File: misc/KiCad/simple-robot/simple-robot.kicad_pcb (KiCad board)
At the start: 2 copper layers, 130 x 81 mm, 38 parts, among them J1 Conn_01x03_Pin, J2 Conn_01x03_Pin, J3 Conn_01x03_Pin, U1 Pico2

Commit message: schematic v2
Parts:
- removed ?: , 
- added C9: 100nF_Ceramic, Capacitor_THT:C_Disc_D5.0mm_W2.5mm_P2.50mm, F.Cu at (63.5, 71.0)
- added J4: Conn_01x03_Pin, Connector_PinHeader_2.54mm:PinHeader_1x03_P2.54mm_Vertical, F.Cu at (57.5, 68.5)
- added REF-MNT: MountingHole_3.7mm_Pad, MountingHole:MountingHole_3.7mm_Pad, F.Cu at (148.5, 105.0)
- moved OLED1 40.1 mm to (130.5, 119.1)
- moved C6 40.0 mm to (126.5, 109.0)
- moved R1 36.3 mm to (146.5, 86.9), turned to 90 degrees
- moved IMU1 36.3 mm to (120.4, 74.0), turned to 180 degrees
- moved C5 32.5 mm to (135.0, 94.5)
- moved TP1 32.0 mm to (133.2, 108.7)
- moved C8 30.6 mm to (131.2, 96.5)
- moved LS_1 30.6 mm to (124.4, 101.7)
- moved C7 29.6 mm to (112.5, 95.5)
- moved BATT1 27.2 mm to (112.8, 113.8), turned to -90 degrees
- moved TP2 23.2 mm to (137.5, 108.8)
- moved C4 20.2 mm to (133.8, 81.5), turned to -90 degrees
- moved C2 15.0 mm to (112.0, 120.0)
- moved C3 14.8 mm to (112.2, 130.8)
- moved S5V1 11.6 mm to (99.7, 121.5)
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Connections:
- U1 pad 7: unconnected-(U1-GPIO5-Pad7)_1 -> Net-(J4-Pin_1)
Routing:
- net Net-(LS_1-LV1): track 253.7 -> 23.8 mm, vias 8 -> 0
- net Net-(LS_1-LV2): track 122.6 -> 18.6 mm, vias 2 -> 0
- net Net-(ENCA1-Pin_3): track 232.1 -> 167.7 mm, vias 2 -> 0
- net Net-(MD1-PWMB): track 113.0 -> 60.3 mm, vias 1 -> 0
- net Net-(IMU1-SCL): track 140.1 -> 88.7 mm, vias 2 -> 0
- net Net-(LS_1-LV4): track 83.2 -> 33.4 mm
- net Net-(IMU1-VCC): track 233.8 -> 199.8 mm, vias 1 -> 2
- net Net-(J4-Pin_1): track 0.00 -> 32.9 mm
- net Net-(LS_1-HV2): track 51.4 -> 20.0 mm, vias 2 -> 0
- net Net-(IMU1-SDA): track 126.5 -> 97.8 mm, vias 3 -> 0
- net Net-(LS_1-HV1): track 52.2 -> 24.4 mm, vias 1 -> 0
- net Net-(LS_1-LV3): track 60.9 -> 33.7 mm, vias 4 -> 0
- net Net-(IMU1-ADD): track 64.1 -> 41.6 mm
- net Net-(MD1-A01): track 48.0 -> 28.4 mm
- net +3V8: track 109.2 -> 90.4 mm
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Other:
- board size 130 x 81 mm -> 99.8 x 81 mm
- board text added: "PWM"
- board text added: "REC"
- board text added: "Servo"
- board text added: "simple-robot 01-2025 rafael v0.2"
- board text removed: "simple-robot 01-2025 rafael v0.1"

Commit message: update schematic and pcb
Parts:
- moved BATT1 37.5 mm to (148.5, 125.2), turned to 0 degrees
- moved C5 8.11 mm to (139.5, 87.8)
- moved C7 4.78 mm to (113.0, 90.8)
- moved R1 3.49 mm to (146.5, 90.4)
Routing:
- net +3V8: track 90.4 -> 138.3 mm, vias 0 -> 2
- net Net-(ENCA1-Pin_3): track 167.7 -> 183.6 mm, vias 0 -> 1
- net Net-(LS_1-HV1): track 24.4 -> 18.2 mm
- net Net-(LS_1-HV4): track 37.0 -> 33.6 mm, vias 1 -> 3
- net Net-(LS_1-HV3): track 31.2 -> 34.3 mm, vias 0 -> 3
- net Net-(MD1-BIN2): track 37.1 -> 39.9 mm
- net Net-(MD1-A02): track 28.4 -> 30.9 mm
- net Net-(MD1-A01): track 28.4 -> 30.8 mm, vias 0 -> 1
- net Net-(LS_1-HV2): track 20.0 -> 22.1 mm
- net Net-(IMU1-VCC): track 199.8 -> 201.8 mm, vias 2 -> 5
- net Net-(MD1-PWMB): track 60.3 -> 62.0 mm
- net Net-(IMU1-SCL): track 88.7 -> 89.9 mm, vias 0 -> 3
- net Net-(MD1-BIN1): track 48.5 -> 49.6 mm
- net Net-(U1-GPIO2): track 19.0 -> 18.1 mm
- net Net-(MD1-AIN2): track 31.9 -> 32.7 mm
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- added copper zone on B.Cu, net GND
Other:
- board text added: "simple-robot 01-2025 v0.3 rafael"
- board text removed: "simple-robot 01-2025 rafael v0.2"

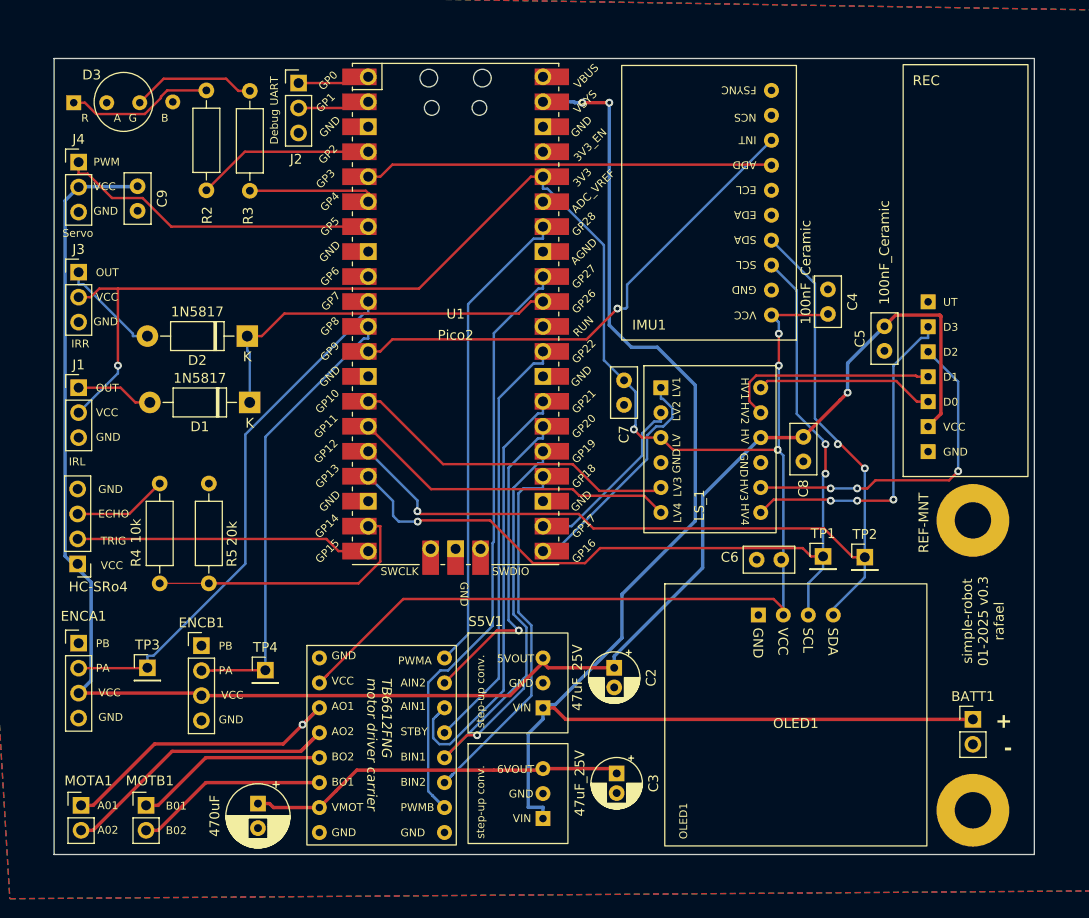
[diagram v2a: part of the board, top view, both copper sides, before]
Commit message: update 3d models for hc-sr04 mount, update KiCad files, update schematic and PCB
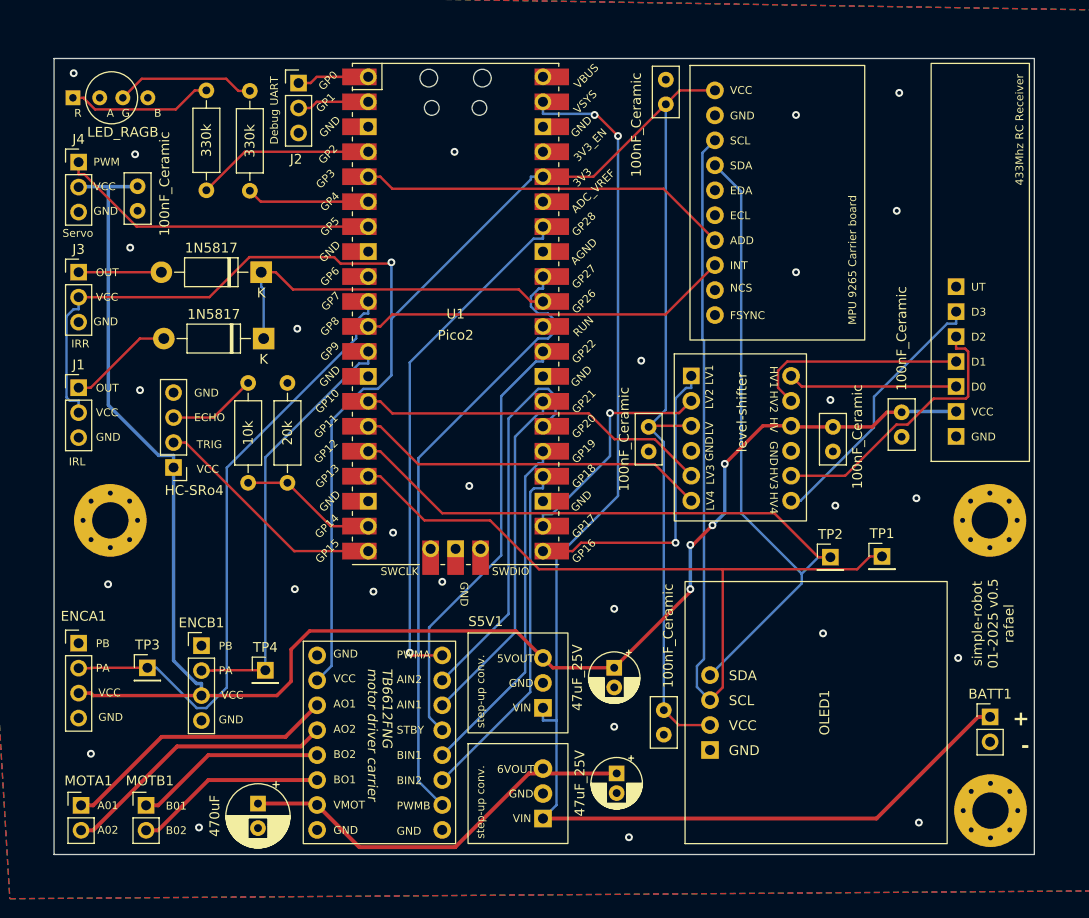
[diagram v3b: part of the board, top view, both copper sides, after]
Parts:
- removed REF**, REF-MNT: MountingHole_3.7mm_Pad, MountingHole:MountingHole_3.7mm_Pad
- added H1: MountingHole_Pad, MountingHole:MountingHole_3.7mm_Pad_Via, F.Cu at (60.7, 105.0)
- added H2: MountingHole_Pad, MountingHole:MountingHole_3.7mm_Pad_Via, F.Cu at (150.3, 134.5)
- added H3: MountingHole_Pad, MountingHole:MountingHole_3.7mm_Pad_Via, F.Cu at (150.2, 105.0)
- moved C4 27.0 mm to (117.2, 60.2)
- moved C6 20.2 mm to (117.0, 126.8), turned to 90 degrees
- moved HC-SRo4 13.8 mm to (67.2, 99.6)
- moved R4 13.6 mm to (74.8, 91.0)
- moved R5 13.0 mm to (78.8, 101.2)
- moved IMU1 9.82 mm to (129.9, 71.4), turned to 0 degrees
- moved C5 8.92 mm to (141.2, 96.5)
- moved D1 6.65 mm to (76.3, 86.5)
- moved D2 6.65 mm to (76.1, 79.8)
- moved OLED1 6.58 mm to (126.8, 124.6), turned to 90 degrees
- moved TP1 6.00 mm to (139.2, 108.7)
- moved C7 5.36 mm to (115.5, 95.5)
- moved TP2 3.50 mm to (134.0, 108.8)
- moved LS_1 3.31 mm to (127.5, 100.5)
- moved R1 3.24 mm to (149.3, 88.8)
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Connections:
- U1 pad 11: Net-(ENCB1-Pin_2) -> Net-(IMU1-INT)
- U1 pad 12: Net-(IMU1-INT) -> Net-(ENCB1-Pin_2)
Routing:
- net Net-(IMU1-SCL): track 89.9 -> 129.0 mm, vias 3 -> 0
- net Net-(IMU1-SDA): track 98.6 -> 114.5 mm, vias 3 -> 0
- net Net-(U1-GPIO14): track 28.2 -> 14.0 mm
- net Net-(MD1-BIN1): track 49.6 -> 35.4 mm, vias 1 -> 0
- net Net-(IMU1-INT): track 51.3 -> 37.9 mm, vias 1 -> 0
- net Net-(MD1-AIN1): track 45.6 -> 35.4 mm
- net Net-(ENCA1-Pin_2): track 54.2 -> 63.2 mm
- net Net-(ENCA1-Pin_3): track 183.6 -> 175.2 mm, vias 1 -> 4
- net Net-(LS_1-LV1): track 23.8 -> 31.8 mm, vias 0 -> 1
- net Net-(IMU1-VCC): track 201.8 -> 209.4 mm, vias 5 -> 1
- net Net-(MD1-AIN2): track 32.7 -> 39.4 mm, vias 1 -> 0
- net Net-(LS_1-HV4): track 33.6 -> 27.3 mm, vias 3 -> 0
- net Net-(LS_1-HV3): track 34.3 -> 28.5 mm, vias 3 -> 0
- net Net-(HC-SRo4-Pin_2): track 30.1 -> 24.4 mm
- net Net-(LS_1-LV2): track 18.6 -> 23.7 mm, vias 0 -> 1
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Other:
- board text added: "433Mhz RC Receiver"
- board text added: "MPU 9265 Carrier board"
- board text added: "level-shifter"
- board text added: "simple-robot 01-2025 v0.5 rafael"
- board text removed: "REC"
- board text removed: "simple-robot 01-2025 v0.3 rafael"

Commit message: Update KiCad project files and remove unnecessary autosave and lock files
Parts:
- removed C7: 100nF_Ceramic, Capacitor_THT:C_Disc_D5.0mm_W2.5mm_P2.50mm
- removed D1, D2: 1N5817, Diode_THT:D_DO-41_SOD81_P10.16mm_Horizontal
- removed J1, J2, J3, J4: Conn_01x03_Pin, Connector_PinHeader_2.54mm:PinHeader_1x03_P2.54mm_Vertical
- removed R4: 10k, Resistor_THT:R_Axial_DIN0207_L6.3mm_D2.5mm_P10.16mm_Horizontal
- removed R5: 20k, Resistor_THT:R_Axial_DIN0207_L6.3mm_D2.5mm_P10.16mm_Horizontal
- removed TP1, TP2, TP3, TP4: Conn_01x01_Pin, Connector_PinHeader_2.54mm:PinHeader_1x01_P2.54mm_Vertical
- added C10: 100nF, Capacitor_THT:C_Disc_D5.0mm_W2.5mm_P2.50mm, F.Cu at (57.6, 94.2)
- added C11: 100nF, Capacitor_THT:C_Disc_D5.0mm_W2.5mm_P2.50mm, F.Cu at (67.0, 125.2)
- added C12: 100nF_Ceramic, Capacitor_THT:C_Disc_D5.0mm_W2.5mm_P2.50mm, F.Cu at (63.5, 125.2)
- added C13: 100nF, Capacitor_THT:C_Disc_D5.0mm_W2.5mm_P2.50mm, F.Cu at (80.8, 83.8)
- added C14: 100nF, Capacitor_THT:C_Disc_D5.0mm_W2.5mm_P2.50mm, F.Cu at (63.8, 83.5)
- added C15: 100nF, Capacitor_THT:C_Disc_D5.0mm_W2.5mm_P2.50mm, F.Cu at (78.2, 121.2)
- added C17: 220uF_10V, Capacitor_THT:CP_Radial_D6.3mm_P2.50mm, F.Cu at (111.5, 118.8)
- added DBG1: Conn_01x03_Pin, Connector_PinHeader_2.54mm:PinHeader_1x03_P2.54mm_Vertical, F.Cu at (80.5, 60.2)
- added IRL1: Conn_01x03_Pin, Connector_PinHeader_2.54mm:PinHeader_1x03_P2.54mm_Vertical, F.Cu at (67.2, 99.5)
- added IRR1: Conn_01x03_Pin, Connector_PinHeader_2.54mm:PinHeader_1x03_P2.54mm_Vertical, F.Cu at (74.0, 99.5)
- added LS_2: ~, common-hobby-things:Level shifter 4 bi-dir, F.Cu at (75.0, 88.7)
- added SERVO1: Conn_01x03_Pin, Connector_PinHeader_2.54mm:PinHeader_1x03_P2.54mm_Vertical, F.Cu at (57.2, 68.5)
- added TPENCA1: Conn_01x01_Pin, Connector_PinHeader_2.54mm:PinHeader_1x01_P2.54mm_Vertical, F.Cu at (57.8, 112.5)
- added TPENCB1: Conn_01x01_Pin, Connector_PinHeader_2.54mm:PinHeader_1x01_P2.54mm_Vertical, F.Cu at (70.8, 112.8)
- added TPGND1: Conn_01x01_Pin, Connector_PinHeader_2.54mm:PinHeader_1x01_P2.54mm_Vertical, F.Cu at (71.8, 130.5)
- added TPGND2: Conn_01x01_Pin, Connector_PinHeader_2.54mm:PinHeader_1x01_P2.54mm_Vertical, F.Cu at (141.0, 62.0)
- added TPSCL1: Conn_01x01_Pin, Connector_PinHeader_2.54mm:PinHeader_1x01_P2.54mm_Vertical, F.Cu at (120.5, 109.0)
- added TPSDA1: Conn_01x01_Pin, Connector_PinHeader_2.54mm:PinHeader_1x01_P2.54mm_Vertical, F.Cu at (127.0, 109.0)
- C2: value 47uF_25V -> 220uF_10V; footprint Capacitor_THT:CP_Radial_D5.0mm_P2.00mm -> Capacitor_THT:CP_Radial_D6.3mm_P2.50mm
- C3: value 47uF_25V -> 100nF; footprint Capacitor_THT:CP_Radial_D5.0mm_P2.00mm -> Capacitor_THT:C_Disc_D5.0mm_W2.5mm_P2.50mm
- C4, C5, C6, C8, C9: value 100nF_Ceramic -> 100nF
- moved C3 41.4 mm to (134.0, 95.5)
- moved C8 18.8 mm to (115.5, 95.2)
- moved HC-SRo4 16.1 mm to (57.5, 86.8)
- moved R3 11.3 mm to (77.6, 60.5), turned to 180 degrees
- moved C2 10.6 mm to (111.5, 130.6)
- moved R2 9.57 mm to (77.5, 64.9), turned to 180 degrees
- moved OLED1 1.35 mm to (125.6, 125.1)
- moved C6 1.06 mm to (116.0, 127.0)
- moved ENCB1 0.75 mm to (70.8, 117.8)
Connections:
- C2 pad 1: Net-(ENCA1-Pin_3) -> Net-(MD1-VMOT)
- C3 pad 1: Net-(MD1-VMOT) -> Net-(ENCA1-Pin_3)
- C4 pad 1: GND -> Net-(IMU1-VCC)
- C4 pad 2: Net-(IMU1-VCC) -> GND
- C5 pad 1: GND -> Net-(ENCA1-Pin_3)
- C5 pad 2: Net-(ENCA1-Pin_3) -> GND
- C8 pad 1: Net-(ENCA1-Pin_3) -> Net-(IMU1-VCC)
- MOTB1 pad 1: Net-(MD1-B02) -> Net-(MD1-B01)
- MOTB1 pad 2: Net-(MD1-B01) -> Net-(MD1-B02)
- R1 pad 3: Net-(LS_1-HV1) -> Net-(LS_1-HV4)
- R1 pad 4: Net-(LS_1-HV2) -> Net-(LS_1-HV3)
- R1 pad 5: Net-(LS_1-HV3) -> Net-(LS_1-HV2)
- R1 pad 6: Net-(LS_1-HV4) -> Net-(LS_1-HV1)
- U1 pad 10: Net-(ENCA1-Pin_2) -> Net-(LS_2-LV2)
- U1 pad 12: Net-(ENCB1-Pin_2) -> Net-(LS_2-LV1)
- U1 pad 13: unconnected-(U1-GND-Pad13) -> GND
- U1 pad 14: Net-(LS_1-LV3) -> Net-(LS_1-LV4)
- U1 pad 15: Net-(LS_1-LV4) -> Net-(LS_1-LV2)
- U1 pad 20: Net-(HC-SRo4-Pin_2) -> Net-(LS_2-LV4)
- U1 pad 21: Net-(LS_1-LV1) -> Net-(LS_1-LV3)
- U1 pad 22: Net-(LS_1-LV2) -> Net-(LS_1-LV1)
- U1 pad 28: unconnected-(U1-GND-Pad28)_1 -> GND
- U1 pad 42: GND -> unconnected-(U1-GND-Pad42)_1
- U1 pad 8: unconnected-(U1-GND-Pad8) -> GND
- U1 pad 9: unconnected-(U1-GPIO6-Pad9)_1 -> Net-(IRL1-Pin_1)
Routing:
- net Net-(IRL1-Pin_1): track 0.00 -> 39.2 mm, vias 0 -> 1
- net Net-(LS_2-LV4): track 0.00 -> 33.7 mm, vias 0 -> 1
- net Net-(IMU1-SCL): track 129.0 -> 96.8 mm
- net Net-(LS_2-LV1): track 0.00 -> 27.1 mm
- net Net-(LS_2-LV2): track 0.00 -> 24.2 mm, vias 0 -> 1
- net Net-(LS_2-LV3): track 14.0 -> 35.2 mm, vias 0 -> 1
- net Net-(ENCA1-Pin_3): track 175.2 -> 194.1 mm, vias 4 -> 1
- net Net-(HC-SRo4-Pin_3): track 9.05 -> 27.9 mm
- net Net-(LS_1-LV3): track 36.0 -> 18.3 mm
- net Net-(IMU1-VCC): track 209.4 -> 195.5 mm, vias 1 -> 3
- net Net-(ENCA1-Pin_2): track 63.2 -> 51.2 mm
- net Net-(D1-A): track 10.7 -> 0.00 mm
- net Net-(LS_1-LV4): track 36.0 -> 46.3 mm
- net Net-(LS_1-LV2): track 23.7 -> 33.9 mm, vias 1 -> 0
- net Net-(IMU1-SDA): track 114.5 -> 104.6 mm, vias 0 -> 2
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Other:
- board text added: "simple-robot 01-2025 v0.6 rafael"
- board text removed: "simple-robot 01-2025 v0.5 rafael"
